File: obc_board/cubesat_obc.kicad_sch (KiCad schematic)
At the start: 16 parts

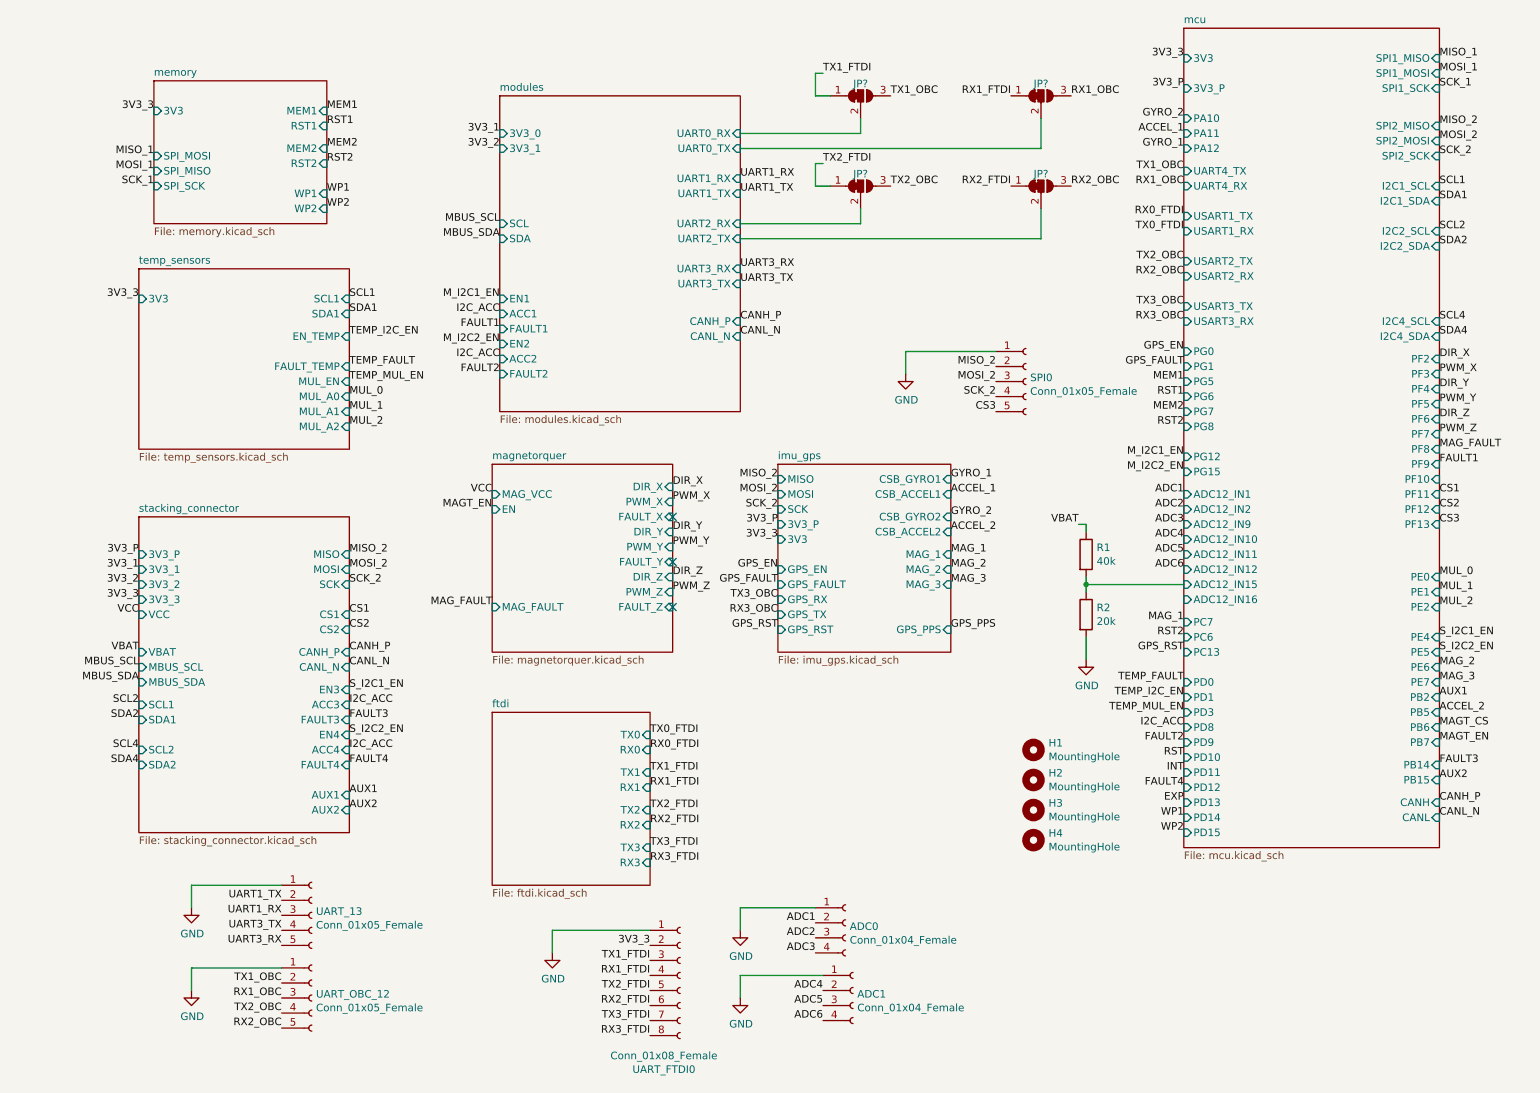
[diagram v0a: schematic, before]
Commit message: changed magnetorquer driver IC and changed power switch IC
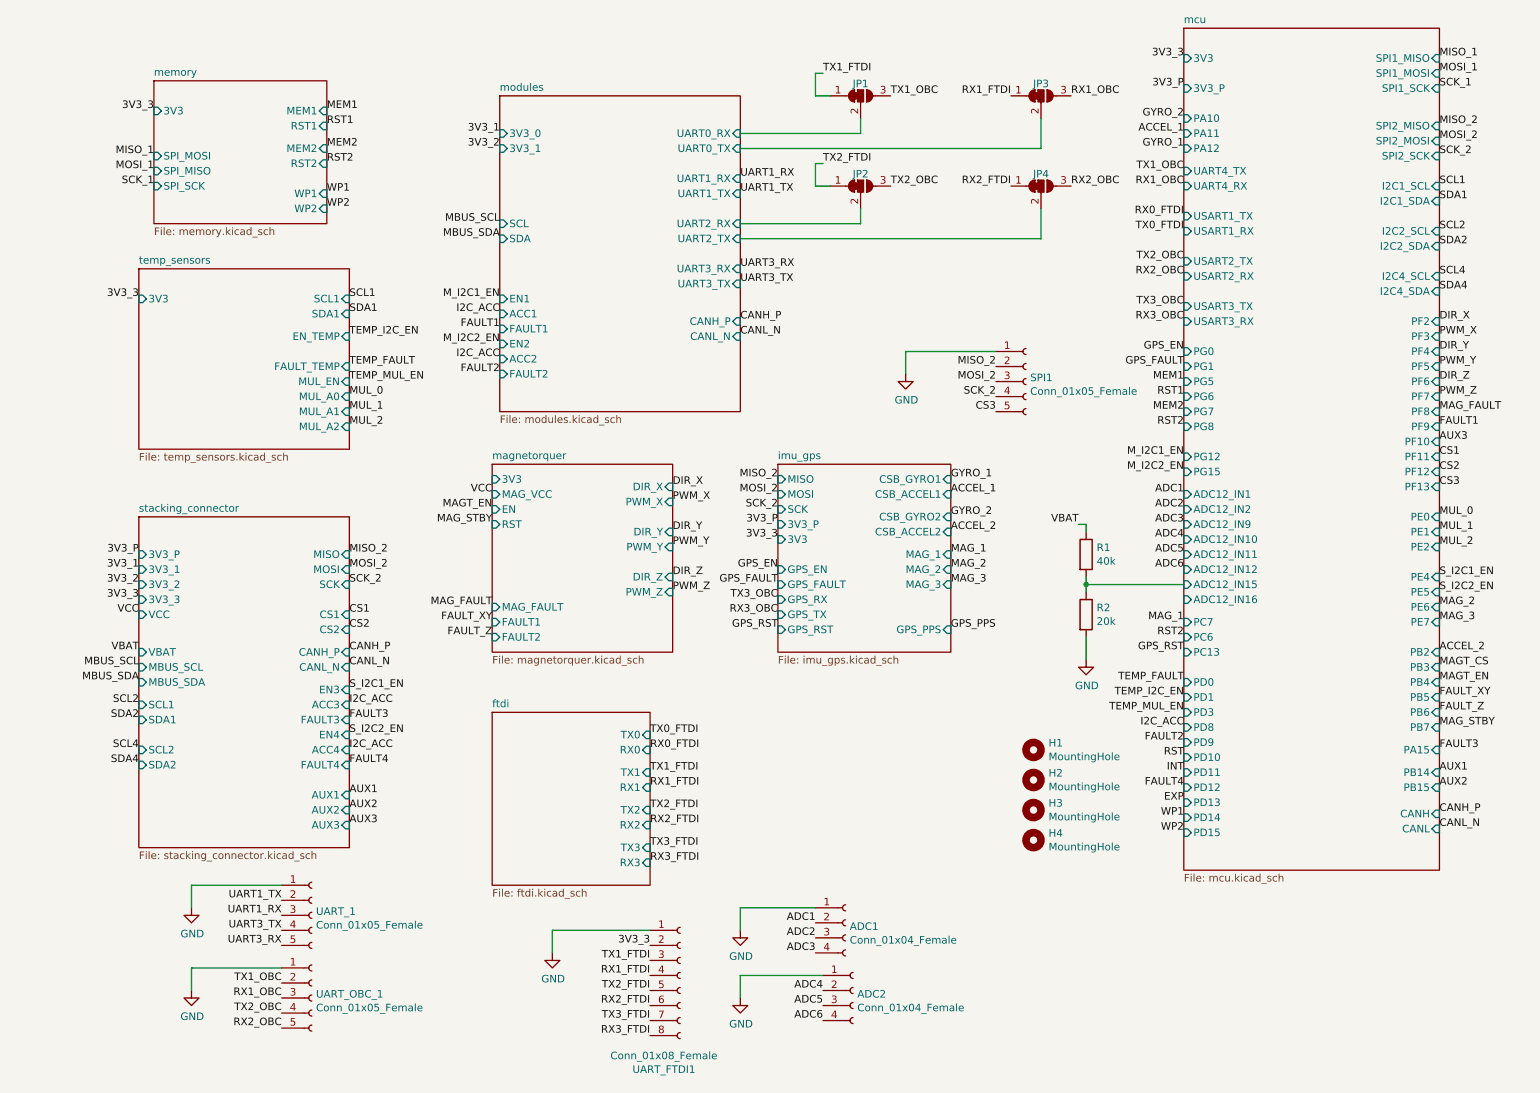
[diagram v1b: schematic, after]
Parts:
- gave numbers to parts that had none: 4
- renumbered ADC0 to ADC1, ADC1 to ADC2, SPI0 to SPI1, UART_13 to UART_1, UART_FTDI0 to UART_FTDI1, UART_OBC_12 to UART_OBC_1
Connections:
- no-connect marks 3 -> 0
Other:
- sheet magnetorquer ports: added 3V3, FAULT1, FAULT2, RST; removed FAULT_X, FAULT_Y, FAULT_Z
- sheet mcu ports: added PA15, PB3, PB4; removed none
- sheet stacking_connector ports: added AUX3; removed none

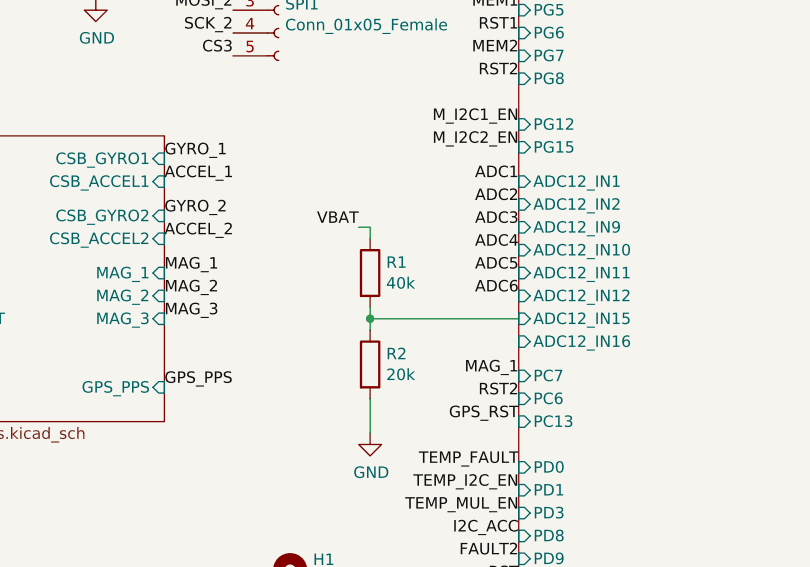
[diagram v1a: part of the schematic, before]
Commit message: updated digikey part numbers and footprints
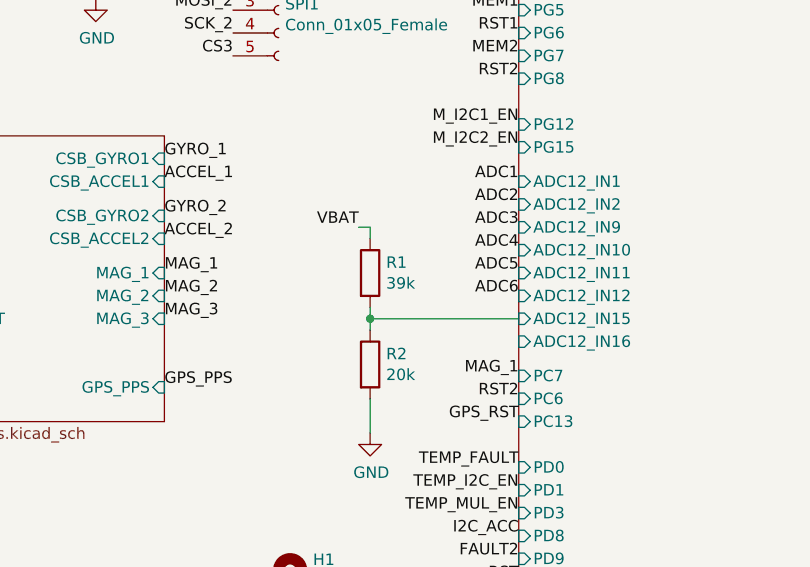
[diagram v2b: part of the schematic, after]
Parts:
- JP1, JP2, JP3, JP4: footprint (none) -> Jumper:SolderJumper-3_P1.3mm_Bridged12_RoundedPad1.0x1.5mm_NumberLabels
- R1: value 40k -> 39k; footprint Resistor_SMD:R_0603_1608Metric -> Resistor_SMD:R_0402_1005Metric; Digikey Part Number PAT40KACT-ND -> YAG2089CT-ND
- R2: Digikey Part Number 764-1399-1-ND -> YAG2114CT-ND
- SPI1, UART_1, UART_OBC_1: Digikey Part Number WM7623CT-ND -> WM26499CT-ND
- UART_FTDI1: Digikey Part Number WM7626CT-ND -> WM26501CT-ND

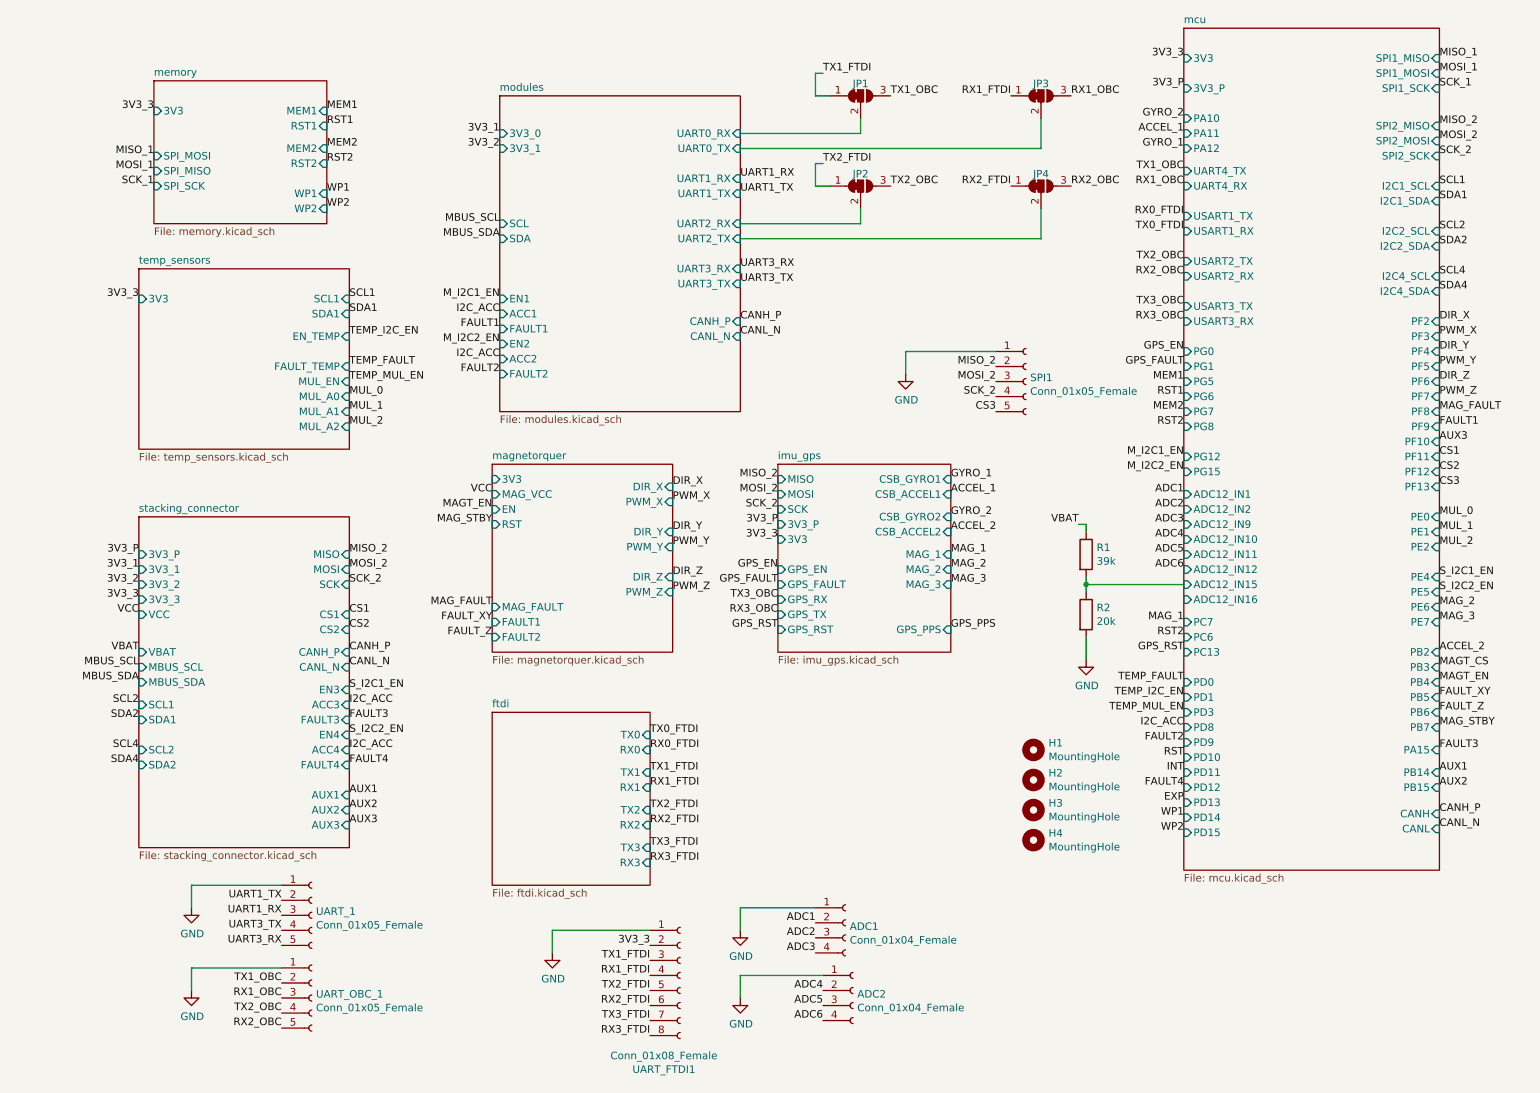
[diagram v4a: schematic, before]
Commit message: routed most of board
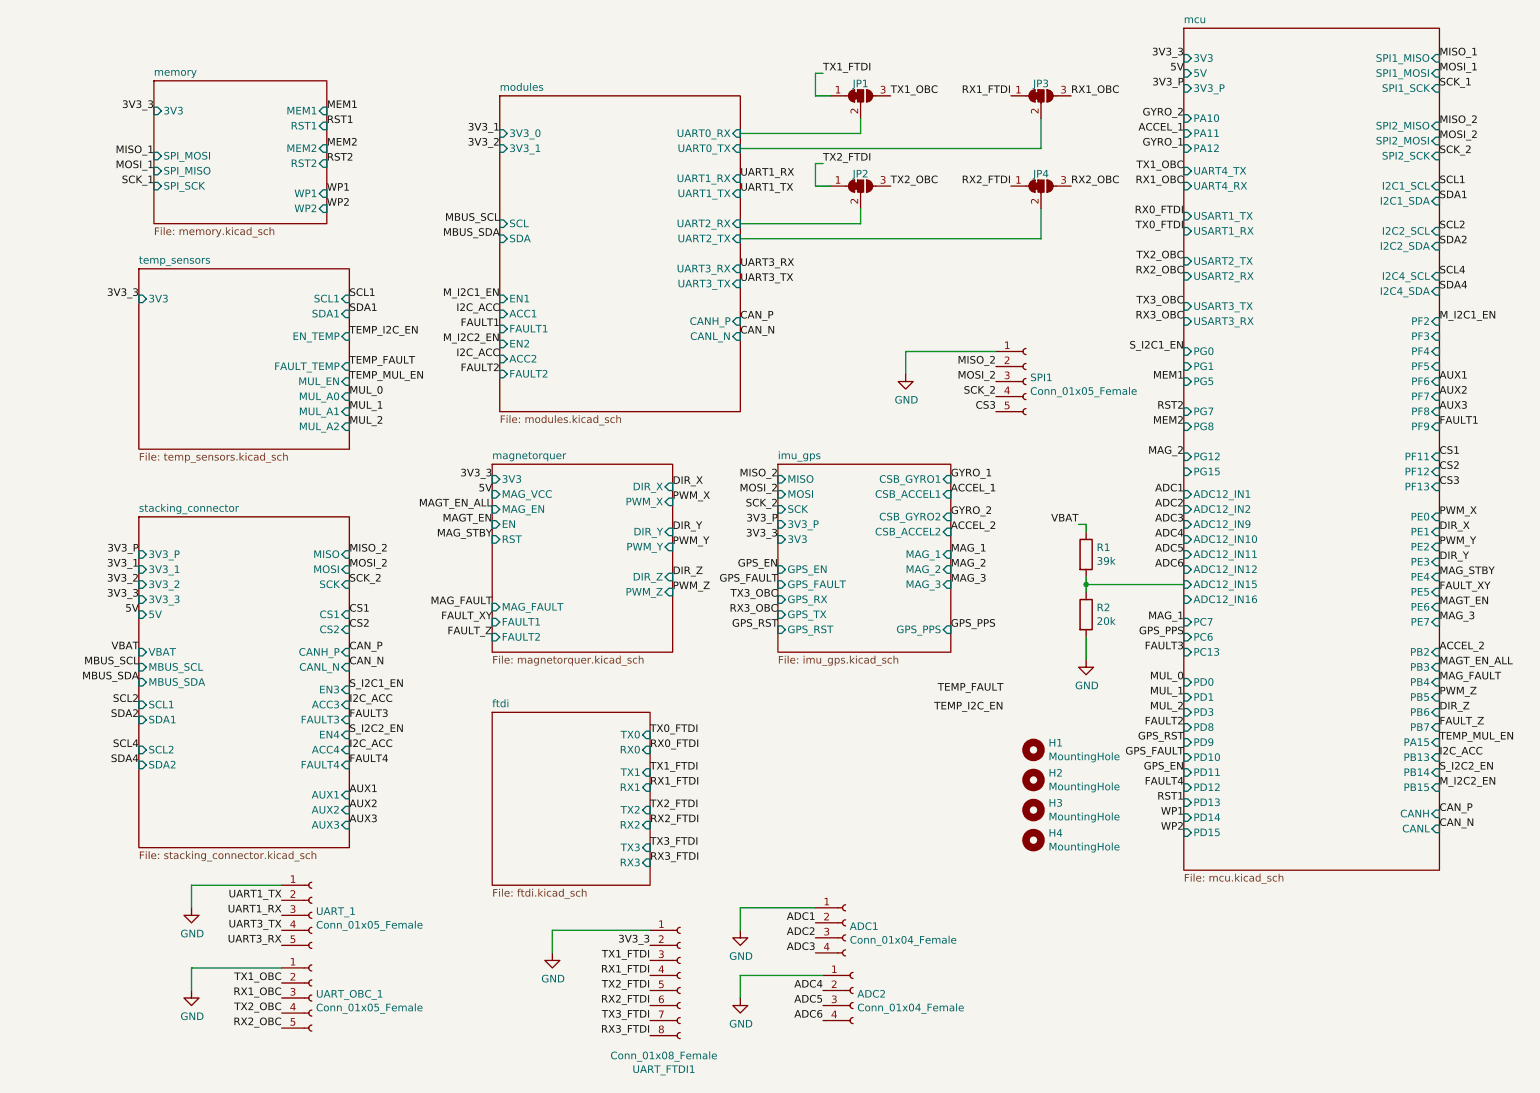
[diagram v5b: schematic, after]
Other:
- sheet magnetorquer ports: added MAG_EN; removed none
- sheet mcu ports: added 5V, PB13, PE3; removed PF10, PG6
- sheet stacking_connector ports: added 5V; removed VCC
